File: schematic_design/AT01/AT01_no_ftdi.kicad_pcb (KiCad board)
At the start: 2 copper layers, 70 x 55 mm, 69 parts, among them J1 JST Connector, J2 USB_C_Receptacle_USB2.0, J3 Conn_01x08, J4 Solenoid Valve Connector, J5 DC Pump Connector, Q1 DMG2301L, Q2 FDS6375, SW1 SW_Push, SW2 SW_Push, SW3 SW_Push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

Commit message: updated FTDI board
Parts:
- moved C3 14.6 mm to (136.0, 74.0), turned to 90 degrees
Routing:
- net Net-(U6-EN): track 37.9 -> 35.3 mm
- net GND: track 60.5 -> 62.5 mm
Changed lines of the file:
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@@
   )
   (footprint "Capacitor_SMD:C_0603_1608Metric_Pad1.08x0.95mm_HandSolder" (layer "F.Cu")
-    (at 122 78.1375 -90)
+    (at 136 74 90)
     (descr "Capacitor SMD 0603 (1608 Metric), square (rectangular) end terminal, IPC_7351 nominal with elongated pad for handsoldering. (Body size source: IPC-SM-782 page 76, https://www.pcb-3d.com/wordpress/wp-content/uploads/ipc-sm-782a_amendment_1_and_2.pdf), generated with kicad-footprint-generator")
     (tags "capacitor handsolder")
@@
     (fp_line (start 0.8 0.4) (end -0.8 0.4)
       (stroke (width 0.1) (type solid)) (layer "F.Fab"))
-    (pad "1" smd roundrect (at -0.8625 0 270) (size 1.075 0.95) (layers "F.Cu" "F.Paste" "F.Mask") (roundrect_rratio 0.25)
+    (pad "1" smd roundrect (at -0.8625 0 90) (size 1.075 0.95) (layers "F.Cu" "F.Paste" "F.Mask") (roundrect_rratio 0.25)
       (net 46 "Net-(U6-EN)") (pintype "passive"))
-    (pad "2" smd roundrect (at 0.8625 0 270) (size 1.075 0.95) (layers "F.Cu" "F.Paste" "F.Mask") (roundrect_rratio 0.25)
+    (pad "2" smd roundrect (at 0.8625 0 90) (size 1.075 0.95) (layers "F.Cu" "F.Paste" "F.Mask") (roundrect_rratio 0.25)
       (net 2 "GND") (pintype "passive"))
     (model "${KICAD6_3DMODEL_DIR}/Capacitor_SMD.3dshapes/C_0603_1608Metric.wrl"
@@
   (segment (start 152.2625 109.0375) (end 152.3 109) (width 0.3) (layer "F.Cu") (net 2))
   (segment (start 141.05 82.88) (end 141.05 81.85) (width 0.3) (layer "F.Cu") (net 2))
+  (segment (start 136 73.1375) (end 134.8625 72) (width 0.52) (layer "F.Cu") (net 2))
   (segment (start 152.325001 115.225001) (end 152.325001 114.0514) (width 0.3) (layer "F.Cu") (net 2))
   (segment (start 155.8625 108.4625) (end 155.8 108.4) (width 0.52) (layer "F.Cu") (net 2))
@@
   (segment (start 127.7 104.38) (end 127.82 104.38) (width 0.3) (layer "F.Cu") (net 2))
   (segment (start 158.55 82.88) (end 158.55 81.55) (width 0.3) (layer "F.Cu") (net 2))
-  (segment (start 122 79) (end 120.6 79) (width 0.3) (layer "F.Cu") (net 2))
+  (segment (start 134.8625 72) (end 133 72) (width 0.52) (layer "F.Cu") (net 2))
   (segment (start 124.445 105.14) (end 124.445 105.295) (width 0.3) (layer "F.Cu") (net 2))
   (segment (start 136 90.725) (end 134.525 90.725) (width 0.3) (layer "F.Cu") (net 2))
@@
   (via (at 127.6 97.1) (size 0.6) (drill 0.3) (layers "F.Cu" "B.Cu") (net 2))
   (via (at 127.6 100.2) (size 0.6) (drill 0.3) (layers "F.Cu" "B.Cu") (net 2))
-  (via (at 120.6 79) (size 0.6) (drill 0.3) (layers "F.Cu" "B.Cu") (net 2))
+  (via (at 133 72) (size 0.6) (drill 0.3) (layers "F.Cu" "B.Cu") (net 2))
   (via (at 164 119.5) (size 0.6) (drill 0.3) (layers "F.Cu" "B.Cu") (net 2))
   (via (at 138.6 94.9) (size 0.6) (drill 0.3) (layers "F.Cu" "B.Cu") (net 2))
@@
   (segment (start 133.6625 74.75) (end 136 77.0875) (width 0.52) (layer "F.Cu") (net 46))
   (segment (start 137.5 78.5875) (end 137.5 79) (width 0.52) (layer "F.Cu") (net 46))
-  (segment (start 125.75 74.75) (end 124.525 74.75) (width 0.52) (layer "F.Cu") (net 46))
-  (segment (start 124.525 74.75) (end 122 77.275) (width 0.52) (layer "F.Cu") (net 46))
+  (segment (start 136 74.8625) (end 136 77.0875) (width 0.52) (layer "F.Cu") (net 46))
   (segment (start 132.25 74.75) (end 133.6625 74.75) (width 0.52) (layer "F.Cu") (net 46))
   (via (at 137.5 79) (size 0.6) (drill 0.3) (layers "F.Cu" "B.Cu") (net 46))

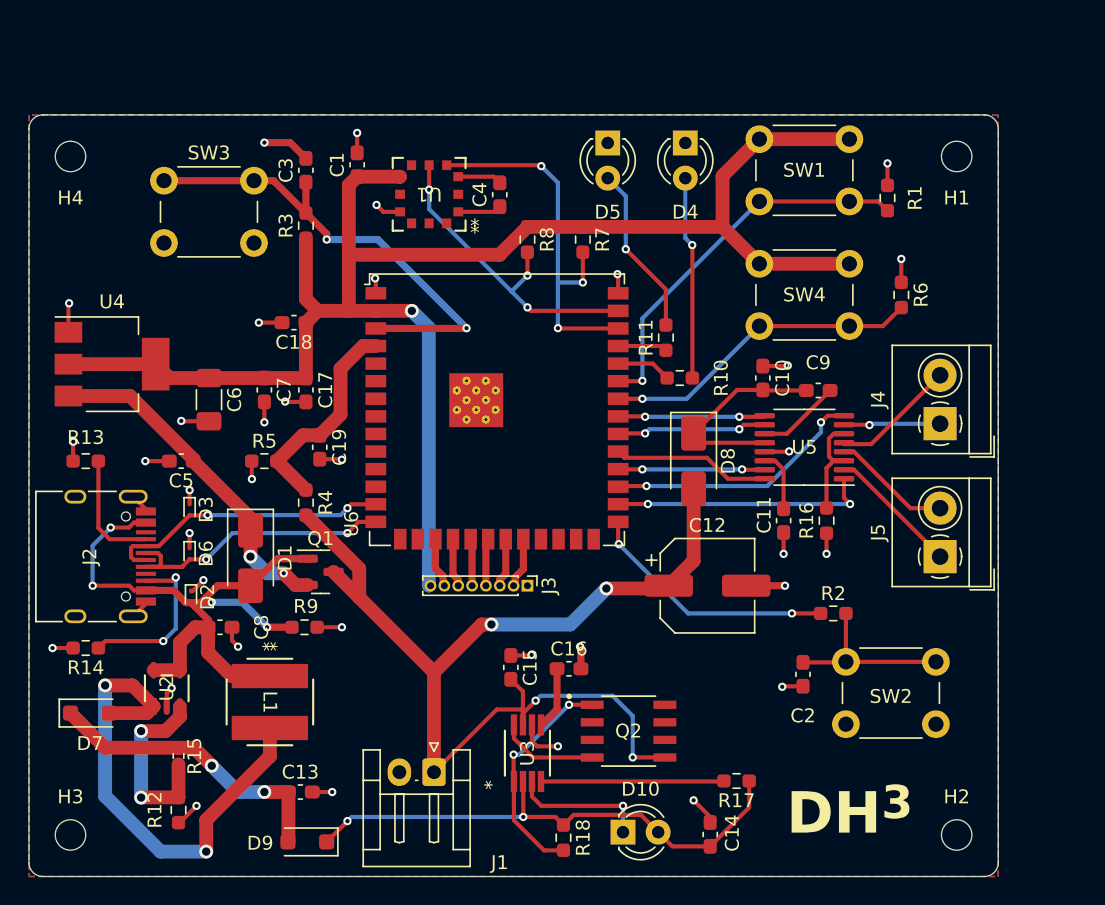
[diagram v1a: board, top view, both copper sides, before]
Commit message: adding design recommendations from call with Yi
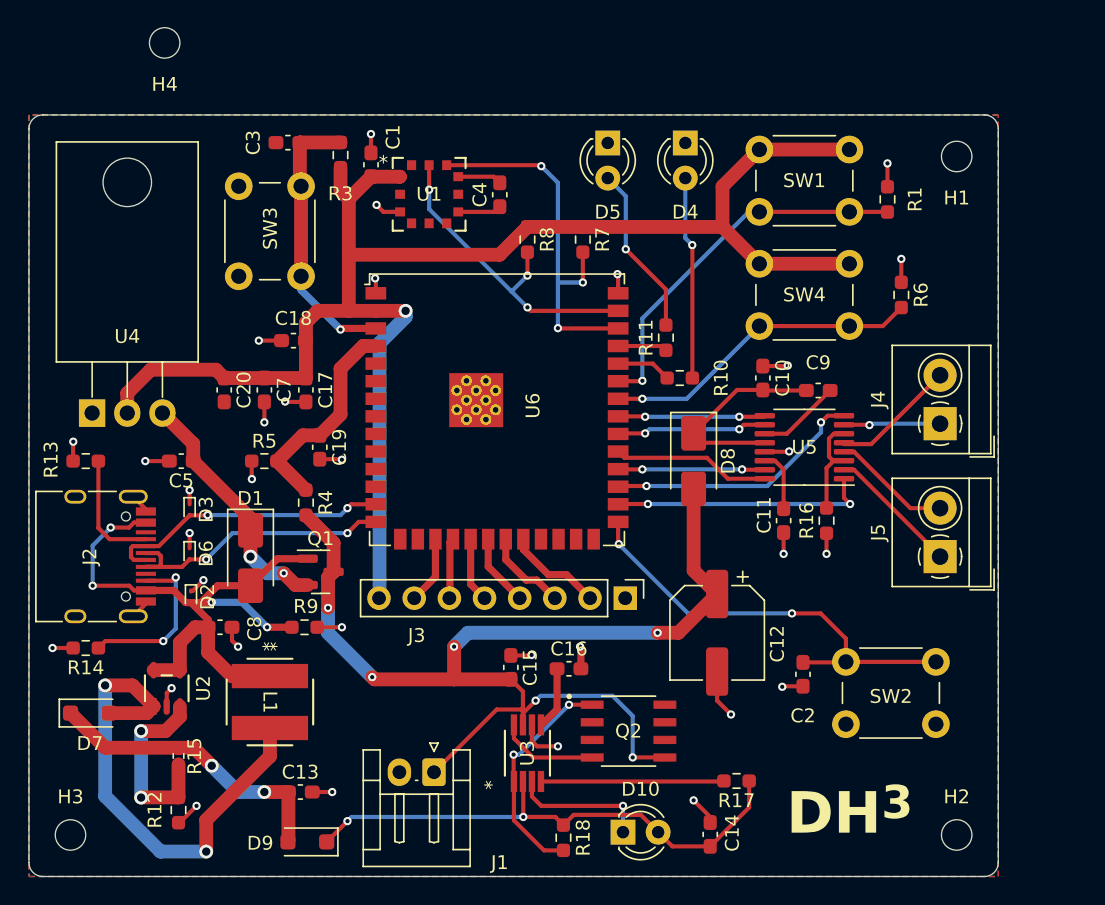
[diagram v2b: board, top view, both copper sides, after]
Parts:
- removed C6: 10uF, Capacitor_SMD:C_1206_3216Metric_Pad1.33x1.80mm_HandSolder
- removed R2: 10K, Resistor_SMD:R_0603_1608Metric_Pad0.98x0.95mm_HandSolder
- added C20: 10uF, Capacitor_SMD:C_0603_1608Metric_Pad1.08x0.95mm_HandSolder, F.Cu at (130.1, 89.9)
- D2: value ESD9B3.3ST5G -> ESD9B5.0ST5G
- J3: footprint Connector_PinHeader_1.00mm:PinHeader_1x08_P1.00mm_Vertical -> Connector_PinHeader_2.54mm:PinHeader_1x08_P2.54mm_Vertical
- R10, R11: value 5.1K -> 2.2K
- R16: value 2.2K -> 0
- U4: value LM1117MP-3.3 -> LM1117T-3.3; footprint Package_TO_SOT_SMD:SOT-223-3_TabPin2 -> Package_TO_SOT_THT:TO-220-3_Horizontal_TabDown
- moved H4 10.7 mm to (125.8, 64.8)
- moved SW3 9.91 mm to (135.7, 75.2), turned to -90 degrees
- moved J3 7.12 mm to (159.1, 104.9)
- moved R3 5.68 mm to (138.5, 72.9)
- moved U4 3.81 mm to (120.6, 91.5)
- moved C12 3.47 mm to (165.7, 107.4), turned to -90 degrees
- moved C3 2.39 mm to (134.7, 72.0), turned to 180 degrees
- moved C18 1.30 mm to (135.1, 86.3)
- moved C1 1.00 mm to (140.7, 73.6)
- moved SW1 0.75 mm to (168.8, 72.5)
- moved R1 0.10 mm to (178.0, 76.1)
- turned U1 to 0 degrees
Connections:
- C2 pad 1: Net-(C2-Pad1) -> Net-(U6-IO0)
- C4 pad 1: Net-(U1-VDD) -> Net-(U1-VO-)
- C4 pad 2: Net-(U1-VSS) -> Net-(U1-VO+)
- SW2 pad 1: Net-(C2-Pad1) -> Net-(U6-IO0)
- U1 pad 10: Net-(U1-VSS) -> GND
- U1 pad 12: Net-(U1-VDD) -> 3V3
- U1 pad 2: unconnected-(U1-MOSI/SDA-Pad2) -> SDA
- U1 pad 3: unconnected-(U1-SCLK/SCL-Pad3) -> SCL
- U1 pad 4: GND -> Net-(U1-VO+)
- U1 pad 6: 3V3 -> Net-(U1-VO-)
- U1 pad 8: SDA -> unconnected-(U1-EOC-Pad8)
- U1 pad 9: SCL -> unconnected-(U1-RES-Pad9)
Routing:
- net Net-(U6-EN): track 35.3 -> 20.2 mm, vias 2 -> 1
- net Net-(U6-IO0): track 18.3 -> 32.1 mm
- net Net-(C2-Pad1): track 13.1 -> 0.00 mm
- net GND: track 62.5 -> 55.7 mm, vias 35 -> 32
- net Net-(D1-K): track 24.6 -> 18.0 mm
- net 3V3: track 120.6 -> 114.6 mm
- net DC_SCREEN: track 3.65 -> 7.02 mm
- net Net-(U1-VSS): track 3.18 -> 0.00 mm
- net Net-(U1-VO+): track 0.00 -> 3.18 mm
- net Net-(U1-VO-): track 0.00 -> 3.16 mm
- net Net-(U1-VDD): track 3.16 -> 0.00 mm
- net VBAT: track 80.5 -> 83.5 mm, vias 4 -> 6
- net RST_SCREEN: track 3.54 -> 6.17 mm
- net SCK: track 3.43 -> 5.44 mm
- net MOSI: track 3.40 -> 4.82 mm
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
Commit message: adding SSR and new ESD protection diodes according to design review
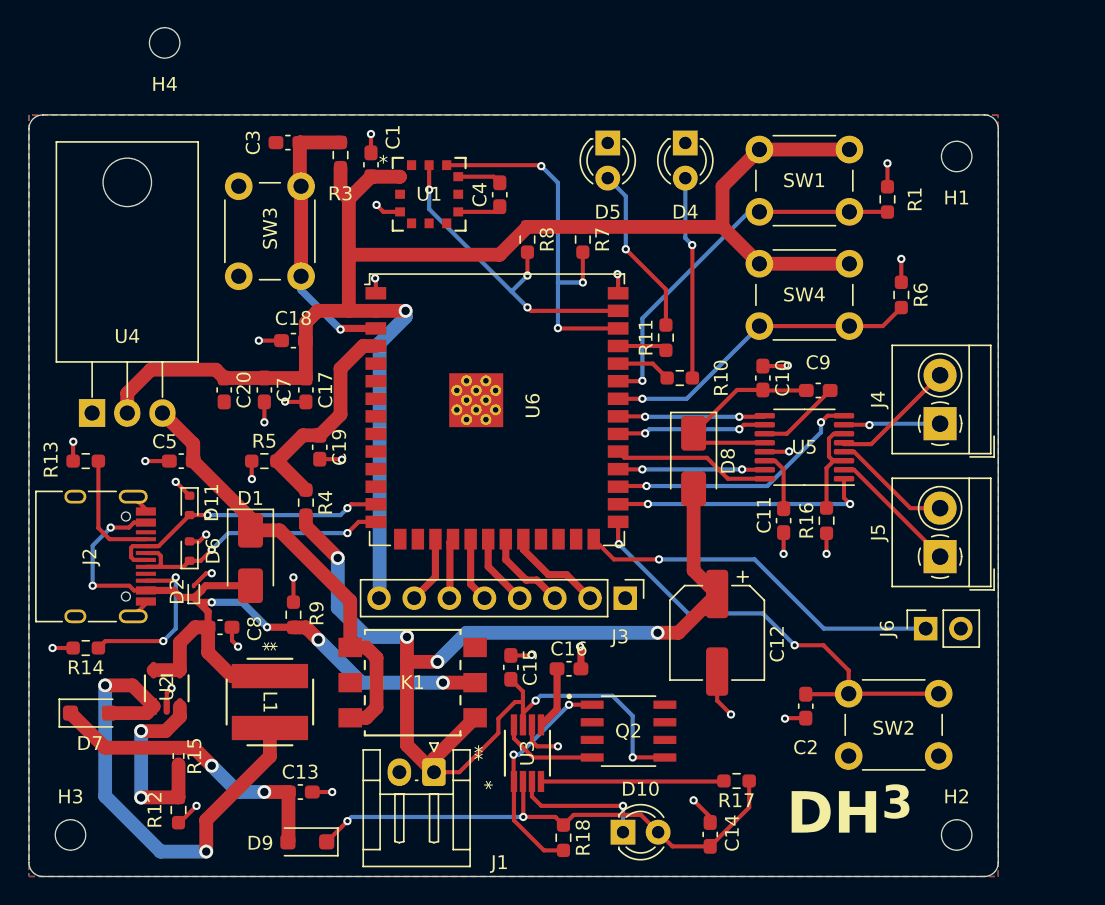
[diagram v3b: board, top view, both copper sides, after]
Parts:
- removed D3: ESD9B3.3ST5G, Diode_SMD:D_SOD-923
- removed Q1: DMG2301L, Package_TO_SOT_SMD:SOT-23
- added D11: PESD3V3S1UB,115, Diode_SMD:D_SOD-523, F.Cu at (127.6, 98.2)
- added J6: PPG Sensor Input, Connector_PinSocket_2.54mm:PinSocket_1x02_P2.54mm_Vertical, F.Cu at (180.8, 107.1)
- added K1: TLP4590ATP1_F, Library:11-7A801S_TOS, F.Cu at (143.7, 111.0)
- D2: value ESD9B5.0ST5G -> ESD9101P2T5G
- D6: value ESD9B3.3ST5G -> PESD3V3S1UB,115; footprint Diode_SMD:D_SOD-923 -> Diode_SMD:D_SOD-523
- R18: value 100m -> 220m
- moved C2 2.31 mm to (172.1, 112.7)
- moved SW2 2.31 mm to (175.2, 111.8)
- moved R9 1.20 mm to (135.1, 106.1), turned to 90 degrees
- moved D2 0.43 mm to (127.9, 104.4), turned to 90 degrees
- moved D6 0.18 mm to (127.6, 101.5), turned to 90 degrees
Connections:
- D2 pad 1: GND -> VBUS
- D2 pad 2: VBUS -> GND
- D6 pad 1: GND -> Net-(D6A-K1)
- D6 pad 2: Net-(D6-A2) -> GND
- J2 pad A6: Net-(D6-A2) -> Net-(D6A-K1)
- J2 pad B6: Net-(D6-A2) -> Net-(D6A-K1)
- U6 pad 14: Net-(D6-A2) -> Net-(D6A-K1)
- U6 pad 26: unconnected-(U6-IO45-Pad26) -> Net-(J6-Pin_1)
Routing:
- net Net-(J6-Pin_1): track 0.00 -> 26.7 mm, vias 0 -> 1
- net Net-(D6-A2): track 20.9 -> 0.00 mm, vias 2 -> 0
- net Net-(D6A-K1): track 0.00 -> 20.9 mm, vias 0 -> 2
- net Net-(D1-K): track 18.0 -> 31.8 mm, vias 2 -> 0
- net VBUS: track 47.8 -> 58.3 mm, vias 4 -> 6
- net VBAT: track 83.5 -> 90.0 mm
- net GND: track 55.7 -> 56.9 mm
- net Net-(U6-IO0): track 32.1 -> 33.2 mm
- net Net-(U6-IO19): track 20.8 -> 21.7 mm

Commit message: added random vias on board for better cap control
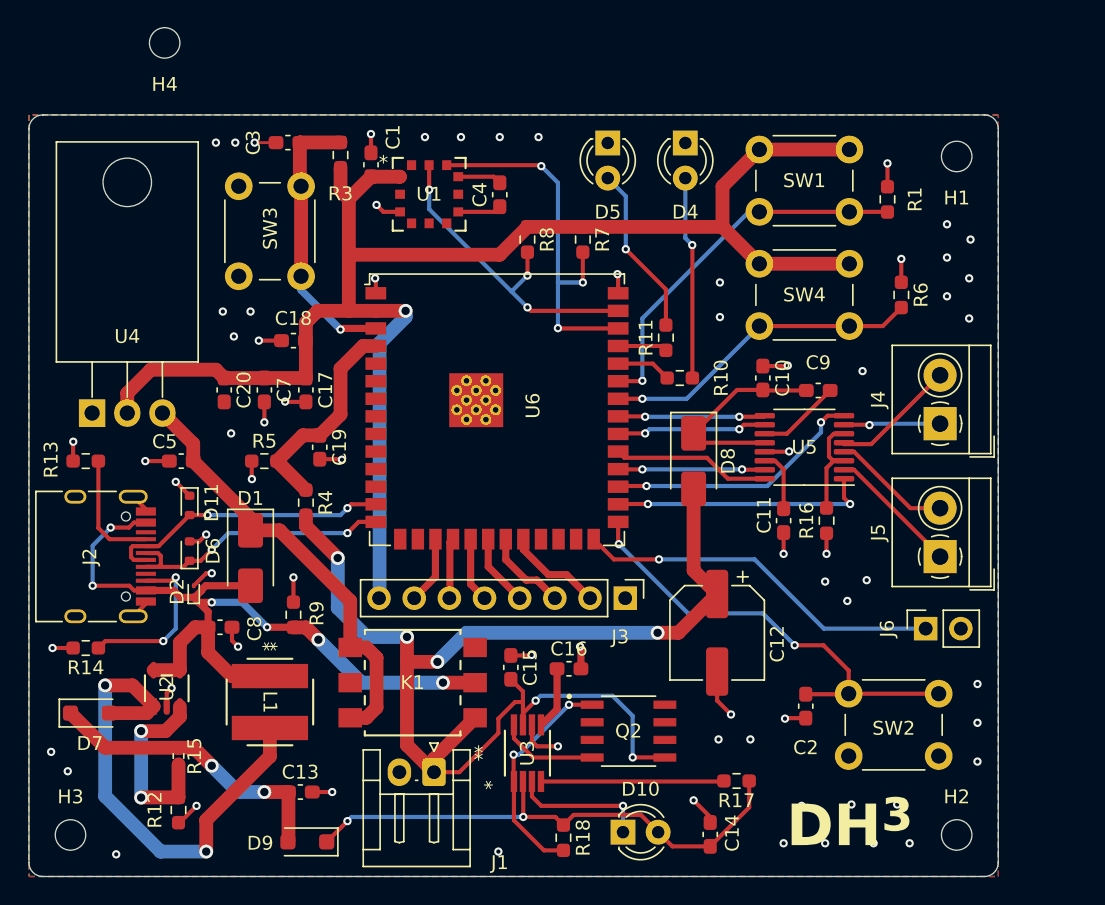
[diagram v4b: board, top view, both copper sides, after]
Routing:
- net GND: track 56.9 -> 58.4 mm, vias 32 -> 71
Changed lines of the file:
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@@
   (gr_line (start 117 70) (end 185 70)
     (stroke (width 0.05) (type default)) (layer "Edge.Cuts"))
-  (gr_text "DH^{3}" (at 170.7 122.2) (layer "F.SilkS")
+  (gr_text "DH^{3}" (at 170.7 123.1) (layer "F.SilkS")
     (effects (font (size 3 3) (thickness 0.6) bold) (justify left bottom))
   )
@@
   (segment (start 124.445 98.64) (end 124.445 98.485) (width 0.3) (layer "F.Cu") (net 2))
   (segment (start 125.950001 111.749999) (end 126.3 111.4) (width 0.3) (layer "F.Cu") (net 2))
+  (segment (start 133.8375 72) (end 132.3 72) (width 0.21) (layer "F.Cu") (net 2))
   (segment (start 141.6 77) (end 141.1 76.5) (width 0.3) (layer "F.Cu") (net 2))
   (segment (start 165.2 121.1) (end 165.2 120.7) (width 0.3) (layer "F.Cu") (net 2))
@@
   (segment (start 142.80011 77) (end 141.6 77) (width 0.3) (layer "F.Cu") (net 2))
   (via (at 126.6 96.5) (size 0.6) (drill 0.3) (layers "F.Cu" "B.Cu") (net 2))
+  (via (at 173.5 103.7) (size 0.6) (drill 0.3) (layers "F.Cu" "B.Cu") (free) (net 2))
   (via (at 152.3 109) (size 0.6) (drill 0.3) (layers "F.Cu" "B.Cu") (net 2))
+  (via (at 173.5 122.6) (size 0.6) (drill 0.3) (layers "F.Cu" "B.Cu") (free) (net 2))
   (via (at 170.5 101.7) (size 0.6) (drill 0.3) (layers "F.Cu" "B.Cu") (net 2))
+  (via (at 168.1 115.1) (size 0.6) (drill 0.3) (layers "F.Cu" "B.Cu") (free) (net 2))
   (via (at 128.8 100.3) (size 0.6) (drill 0.3) (layers "F.Cu" "B.Cu") (net 2))
   (via (at 164 119.5) (size 0.6) (drill 0.3) (layers "F.Cu" "B.Cu") (net 2))
@@
   (via (at 117.7 108.5) (size 0.6) (drill 0.3) (layers "F.Cu" "B.Cu") (net 2))
   (via (at 155.8 108.4) (size 0.6) (drill 0.3) (layers "F.Cu" "B.Cu") (net 2))
+  (via (at 178.7 119.8) (size 0.6) (drill 0.3) (layers "F.Cu" "B.Cu") (free) (net 2))
+  (via (at 165.8 115.1) (size 0.6) (drill 0.3) (layers "F.Cu" "B.Cu") (free) (net 2))
+  (via (at 184.5 111.1) (size 0.6) (drill 0.3) (layers "F.Cu" "B.Cu") (free) (net 2))
+  (via (at 175.4 119.8) (size 0.6) (drill 0.3) (layers "F.Cu" "B.Cu") (free) (net 2))
   (via (at 132.6 86.3) (size 0.6) (drill 0.3) (layers "F.Cu" "B.Cu") (net 2))
   (via (at 124.4 95) (size 0.6) (drill 0.3) (layers "F.Cu" "B.Cu") (net 2))
   (via (at 140.7 71.38125) (size 0.6) (drill 0.3) (layers "F.Cu" "B.Cu") (net 2))
+  (via (at 176.2 88.5) (size 0.6) (drill 0.3) (layers "F.Cu" "B.Cu") (free) (net 2))
+  (via (at 165.9 82.1) (size 0.6) (drill 0.3) (layers "F.Cu" "B.Cu") (free) (net 2))
+  (via (at 130.9 72) (size 0.6) (drill 0.3) (layers "F.Cu" "B.Cu") (free) (net 2))
+  (via (at 183.9 84.7) (size 0.6) (drill 0.3) (layers "F.Cu" "B.Cu") (free) (net 2))
+  (via (at 182.3 80.3) (size 0.6) (drill 0.3) (layers "F.Cu" "B.Cu") (free) (net 2))
   (via (at 170.9 94.3) (size 0.6) (drill 0.3) (layers "F.Cu" "B.Cu") (net 2))
   (via (at 154.2 115.6) (size 0.6) (drill 0.3) (layers "F.Cu" "B.Cu") (net 2))
+  (via (at 183.9 81.8) (size 0.6) (drill 0.3) (layers "F.Cu" "B.Cu") (free) (net 2))
   (via (at 178 73.5) (size 0.6) (drill 0.3) (layers "F.Cu" "B.Cu") (net 2))
+  (via (at 130.8 86) (size 0.6) (drill 0.3) (layers "F.Cu" "B.Cu") (free) (net 2))
+  (via (at 147.2 71.6) (size 0.6) (drill 0.3) (layers "F.Cu" "B.Cu") (free) (net 2))
   (via (at 170.8 88.1) (size 0.6) (drill 0.3) (layers "F.Cu" "B.Cu") (net 2))
+  (via (at 171.8 119.9) (size 0.6) (drill 0.3) (layers "F.Cu" "B.Cu") (free) (net 2))
   (via (at 170.6 113.6) (size 0.6) (drill 0.3) (layers "F.Cu" "B.Cu") (net 2))
+  (via (at 132 84.2) (size 0.6) (drill 0.3) (layers "F.Cu" "B.Cu") (free) (net 2))
   (via (at 141 81.8) (size 0.6) (drill 0.3) (layers "F.Cu" "B.Cu") (net 2))
+  (via (at 118.8 117.4) (size 0.6) (drill 0.3) (layers "F.Cu" "B.Cu") (free) (net 2))
+  (via (at 130 84.2) (size 0.6) (drill 0.3) (layers "F.Cu" "B.Cu") (free) (net 2))
+  (via (at 177 122.6) (size 0.6) (drill 0.3) (layers "F.Cu" "B.Cu") (free) (net 2))
+  (via (at 144.6 71.6) (size 0.6) (drill 0.3) (layers "F.Cu" "B.Cu") (free) (net 2))
   (via (at 166.7 113.3) (size 0.6) (drill 0.3) (layers "F.Cu" "B.Cu") (net 2))
+  (via (at 117.6 116) (size 0.6) (drill 0.3) (layers "F.Cu" "B.Cu") (free) (net 2))
   (via (at 126.3 111.4) (size 0.6) (drill 0.3) (layers "F.Cu" "B.Cu") (net 2))
   (via (at 141.1 76.5) (size 0.6) (drill 0.3) (layers "F.Cu" "B.Cu") (net 2))
+  (via (at 150 71.6) (size 0.6) (drill 0.3) (layers "F.Cu" "B.Cu") (free) (net 2))
   (via (at 133 92.2) (size 0.6) (drill 0.3) (layers "F.Cu" "B.Cu") (net 2))
   (via (at 135.1 103.4) (size 0.6) (drill 0.3) (layers "F.Cu" "B.Cu") (net 2))
   (via (at 137.9 118.9) (size 0.6) (drill 0.3) (layers "F.Cu" "B.Cu") (net 2))
+  (via (at 152.8 71.6) (size 0.6) (drill 0.3) (layers "F.Cu" "B.Cu") (free) (net 2))
+  (via (at 170.5 122.6) (size 0.6) (drill 0.3) (layers "F.Cu" "B.Cu") (free) (net 2))
   (via (at 128.1 119.9) (size 0.6) (drill 0.3) (layers "F.Cu" "B.Cu") (net 2))
+  (via (at 176.5 103.6) (size 0.6) (drill 0.3) (layers "F.Cu" "B.Cu") (free) (net 2))
+  (via (at 175.1 105.1) (size 0.6) (drill 0.3) (layers "F.Cu" "B.Cu") (free) (net 2))
+  (via (at 132.3 72) (size 0.6) (drill 0.3) (layers "F.Cu" "B.Cu") (net 2))
+  (via (at 184.5 116.7) (size 0.6) (drill 0.3) (layers "F.Cu" "B.Cu") (free) (net 2))
+  (via (at 182.3 77.9) (size 0.6) (drill 0.3) (layers "F.Cu" "B.Cu") (free) (net 2))
   (via (at 132.1 96.3) (size 0.6) (drill 0.3) (layers "F.Cu" "B.Cu") (net 2))
+  (via (at 149.9 123.2) (size 0.6) (drill 0.3) (layers "F.Cu" "B.Cu") (free) (net 2))
+  (via (at 122.3 123.4) (size 0.6) (drill 0.3) (layers "F.Cu" "B.Cu") (free) (net 2))
+  (via (at 165.9 84.6) (size 0.6) (drill 0.3) (layers "F.Cu" "B.Cu") (free) (net 2))
   (via (at 119.2 93.6) (size 0.6) (drill 0.3) (layers "F.Cu" "B.Cu") (net 2))
+  (via (at 182.3 83.1) (size 0.6) (drill 0.3) (layers "F.Cu" "B.Cu") (free) (net 2))
   (via (at 129.2 103.1) (size 0.6) (drill 0.3) (layers "F.Cu" "B.Cu") (net 2))
+  (via (at 184 79) (size 0.6) (drill 0.3) (layers "F.Cu" "B.Cu") (free) (net 2))
+  (via (at 129.5 72) (size 0.6) (drill 0.3) (layers "F.Cu" "B.Cu") (free) (net 2))
+  (via (at 179.6 122.6) (size 0.6) (drill 0.3) (layers "F.Cu" "B.Cu") (free) (net 2))
   (via (at 179 80.4) (size 0.6) (drill 0.3) (layers "F.Cu" "B.Cu") (net 2))
+  (via (at 184.5 113.9) (size 0.6) (drill 0.3) (layers "F.Cu" "B.Cu") (free) (net 2))
   (via (at 131.1 108.4) (size 0.6) (drill 0.3) (layers "F.Cu" "B.Cu") (net 2))
+  (via (at 130.6 93) (size 0.6) (drill 0.3) (layers "F.Cu" "B.Cu") (free) (net 2))
   (segment (start 151.674999 111.637499) (end 150.8 110.7625) (width 0.3) (layer "F.Cu") (net 3))
   (segment (start 161.92 116.4) (end 161.925 116.405) (width 0.3) (layer "F.Cu") (net 3))
